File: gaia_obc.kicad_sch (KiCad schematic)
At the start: 36 parts, among them J1 USB_C_Receptacle_USB2.0_16P, J2 Micro_SD_Card_Det2, J3 Conn_01x02_Pin, J6 Conn_01x10_Pin, J7 Conn_01x10_Pin, Q1 FS8205A, U1 CD-PA1616D, U2 LGS4056H, U3 DW01A, U4 USBLC6-2P6, U5 AP2112K-3.3, U6 ESP32-S3-PICO-1-N8R2, U7 WLR089U0-I_RM

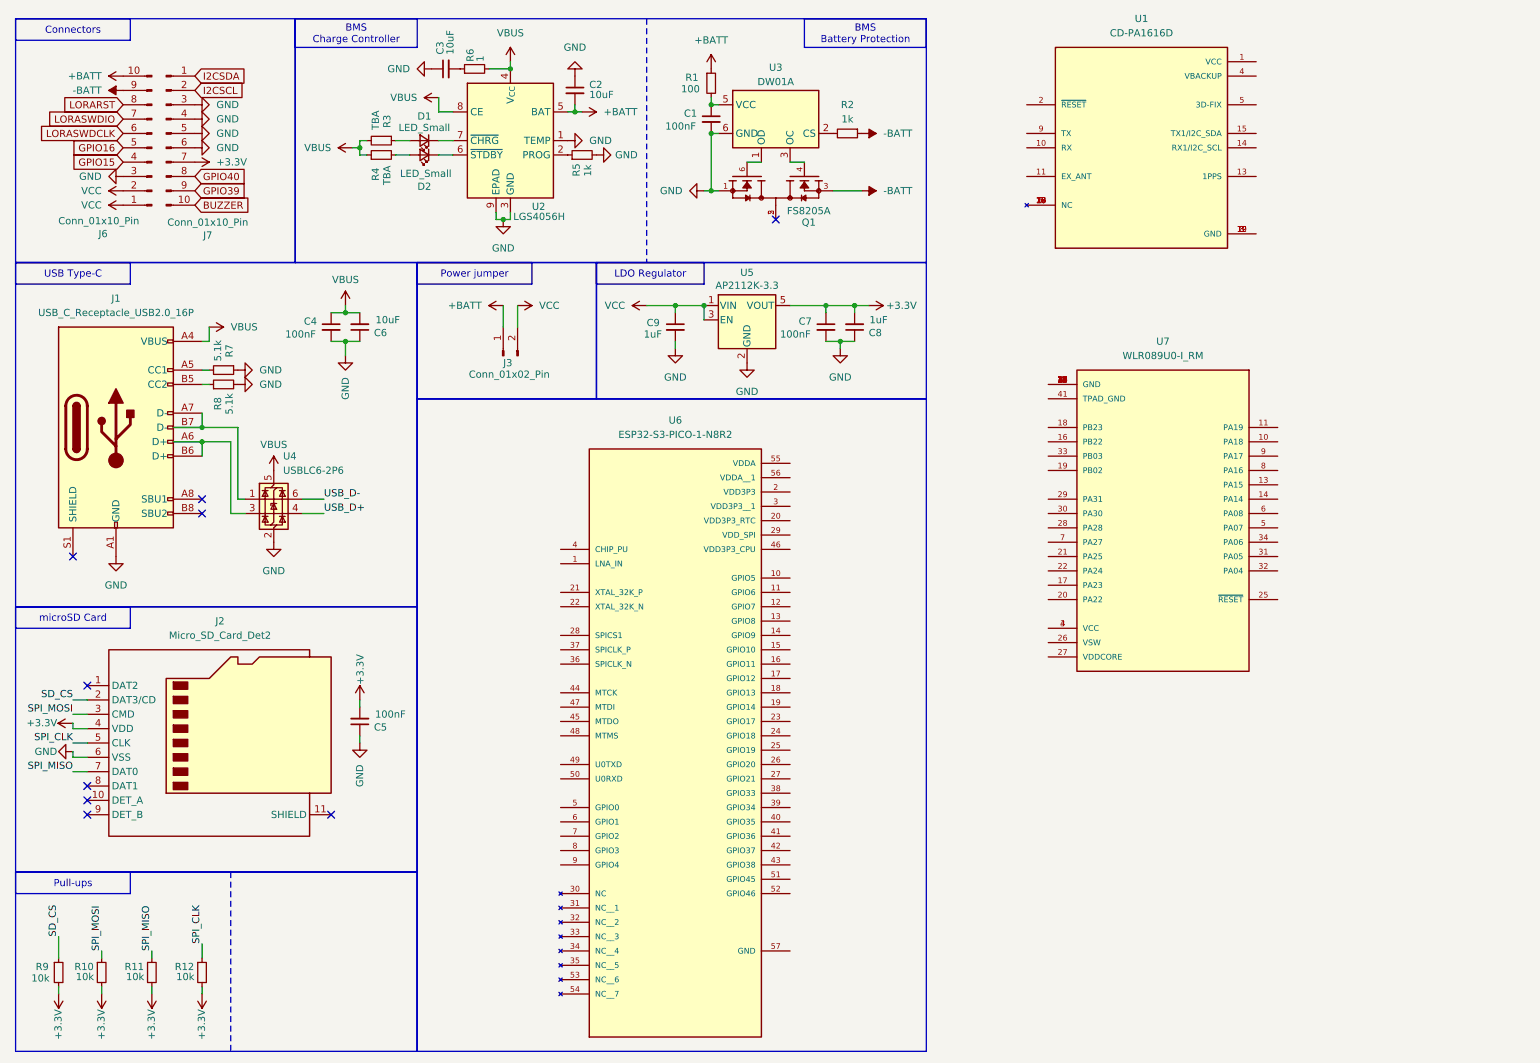
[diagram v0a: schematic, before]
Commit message: creating different sheets
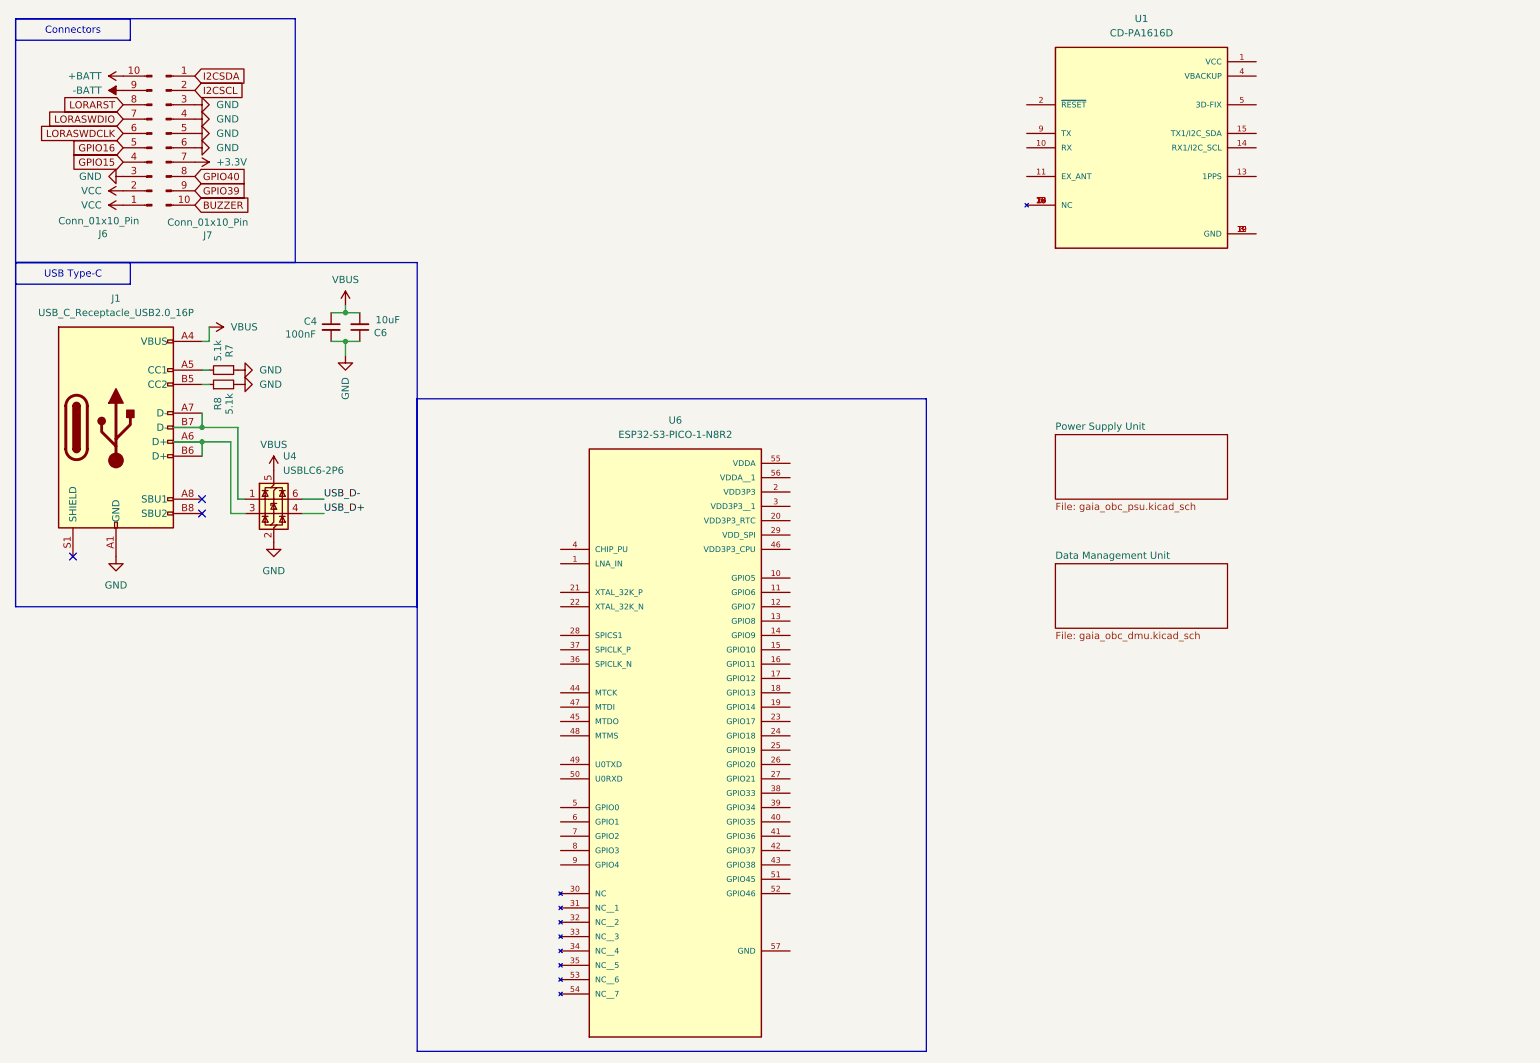
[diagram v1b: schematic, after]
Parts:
- removed C1, C5, C7: 100nF, symbol Device:C_Small
- removed C2, C3: 10uF, symbol Device:C_Small
- removed C8, C9: 1uF, symbol Device:C_Small
- removed D1, D2: LED_Small, symbol Device:LED_Small
- removed J2: Micro_SD_Card_Det2, Connector_Card:microSD_HC_Hirose_DM3D-SF, symbol Connector:Micro_SD_Card_Det2
- removed J3: Conn_01x02_Pin, Connector_Molex:Molex_MicroClasp_55935-0230_1x02_P2.00mm_Horizontal, symbol Connector:Conn_01x02_Pin
- removed Q1: FS8205A, Package_TO_SOT_SMD:SOT-23-6, symbol OnionSAT_Gaia:FS8205A
- removed R1: 100, symbol Device:R_Small
- removed R10, R11, R12, R9: 10k, symbol Device:R_Small
- removed R2, R5: 1k, symbol Device:R_Small
- removed R3, R4: TBA, symbol Device:R_Small
- removed R6: 1, symbol Device:R_Small
- removed U2: LGS4056H, Package_DFN_QFN:DFN-8-1EP_3x3mm_P0.65mm_EP1.7x2.05mm, symbol OnionSAT_Gaia:LGS4056H
- removed U3: DW01A, Package_TO_SOT_SMD:SOT-23-6, symbol Battery_Management:DW01A
- removed U5: AP2112K-3.3, Package_TO_SOT_SMD:SOT-23-5, symbol Regulator_Linear:AP2112K-3.3
- removed U7: WLR089U0-I_RM, OnionSAT_Gaia:MODULE_WLR089U0-I_RM, symbol cs25_onionsat:WLR089U0-I_RM
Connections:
- no-connect marks 9 -> 3
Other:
- added sheet Data Management Unit (gaia_obc_dmu.kicad_sch)
- added sheet Power Supply Unit (gaia_obc_psu.kicad_sch)

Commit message: almost final release
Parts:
- removed J6, J7: Conn_01x10_Pin, Connector_PinHeader_2.54mm:PinHeader_1x10_P2.54mm_Vertical_SMD_Pin1Left, symbol Connector:Conn_01x10_Pin
- removed U1: CD-PA1616D, OnionSAT_Gaia:XCVR_CD-PA1616D, symbol OnionSAT_Gaia:CD-PA1616D
- removed U6: ESP32-S3-PICO-1-N8R2, OnionSAT_Gaia:PQFN40P700X700X106-57N, symbol ESP32-S3-PICO-1-N8R2:ESP32-S3-PICO-1-N8R2
- added BZ1: Buzzer, symbol Device:Buzzer
- added C1, C10, C11, C3, C5, C7, C8, C9: 100nF, Capacitor_SMD:C_0402_1005Metric, symbol Device:C_Small
- added C12, C6: 1uF, Capacitor_SMD:C_0402_1005Metric, symbol Device:C_Small
- added J2, J3: Conn_02x10_Odd_Even, Connector_PinHeader_2.00mm:PinHeader_2x10_P2.00mm_Vertical_SMD, symbol Connector_Generic:Conn_02x10_Odd_Even
- added R1, R10, R11, R12, R13, R2, R3, R6, R7, R8, R9: 10k, symbol Device:R_Small
- added SW1, SW2: SW_Push, symbol Switch:SW_Push
- added U2: MCP23017_ML, Package_DFN_QFN:QFN-28-1EP_6x6mm_P0.65mm_EP4.25x4.25mm, symbol Interface_Expansion:MCP23017_ML
- added U3: ESP32-S3-PICO-1-N8R2, gaia_obc-footprints:PQFN40P700X700X106-57N, symbol gaia_obc-symbols:ESP32-S3-PICO-1-N8R2
- C2: renamed from C4; footprint (none) -> Capacitor_SMD:C_0402_1005Metric
- C4: renamed from C6; footprint (none) -> Capacitor_SMD:C_0402_1005Metric
- renumbered R7 to R4, R8 to R5, U4 to U1
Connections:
- net +3.3V: now also C1.2, C10.1, C11.1, C12.1, C3.1, C7.1, C8.1, C9.1, R1.1, R10.2, R11.2, R12.2, R13.2, R2.1, R3.1, R6.1, R7.2, R8.2, R9.2, U2.5 (VDD), U3.2 (VDD3P3), U3.20 (VDD3P3_RTC), U3.3 (VDD3P3), U3.46 (VDD3P3_CPU), U3.55 (VDDA), U3.56 (VDDA)
- net GND: now also BZ1.2 (-), C1.1, C10.2, C11.2, C12.2, C3.2, C5.1, C6.2, C7.2, C8.2, C9.2, SW1.1, SW2.1, U2.11 (A0), U2.12 (A1), U2.13 (A2), U2.29 (EP), U2.6 (VSS), U3.57 (GND)
- net USB_D+: now also U3.26 (GPIO20)
- net USB_D-: now also U3.25 (GPIO19)
- new net: BZ1.1 (+), U3.24 (GPIO18)
- new net: R3.2, U2.14 (~{RESET})
- new net: R1.2, U2.15 (INTB)
- new net: R2.2, U2.16 (INTA)
- new net: C5.2, C6.1, R6.2, SW1.2, U3.4 (CHIP_PU)
- new net: SW2.2, U3.5 (GPIO0)
- new net: U3.30 (NC), U3.31 (NC), U3.32 (NC), U3.33 (NC), U3.34 (NC), U3.35 (NC), U3.53 (NC), U3.54 (NC)
- new net EN_A1: U2.17 (GPA0)
- new net EN_A2: U2.18 (GPA1)
- new net EN_A3: U2.19 (GPA2)
- new net EN_B1: U2.20 (GPA3)
- new net EN_B2: U2.21 (GPA4)
- new net GPS_RX: U3.6 (GPIO1)
- new net GPS_TX: U3.7 (GPIO2)
- new net I2C_1_SCL: J2.4 (Pin_4), R8.1, U2.8 (SCK), U3.14 (GPIO9)
- new net I2C_1_SDA: J2.2 (Pin_2), R7.1, U2.9 (SDA), U3.13 (GPIO8)
- new net I2C_2_SCL: J2.3 (Pin_3), R12.1, U3.16 (GPIO11)
- new net I2C_2_SDA: J2.1 (Pin_1), R10.1, U3.15 (GPIO10)
- new net LORA_CS: U3.27 (GPIO21)
- new net LORA_RESET: U3.38 (GPIO33)
- new net PB1: U2.25 (GPB0)
- new net PB2: U2.26 (GPB1)
- new net PB3: U2.27 (GPB2)
- new net PB4: U2.28 (GPB3)
- new net PB5: U2.1 (GPB4)
- new net SCREEN_CLK: U3.9 (GPIO4)
- new net SCREEN_CS: U3.10 (GPIO5)
- new net SCREEN_DC: U3.12 (GPIO7)
- new net SCREEN_MOSI: U3.11 (GPIO6)
- new net SCREEN_RESET: U3.8 (GPIO3)
- new net SD_CS: U3.23 (GPIO17)
- new net SPI_0_MISO: R9.1, U3.17 (GPIO12)
- new net SPI_0_MOSI: R11.1, U3.18 (GPIO13)
- new net SPI_0_SCLK: R13.1, U3.19 (GPIO14)
- no-connect marks 3 -> 14
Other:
- sheet Data Management Unit ports: added GPS_RX, GPS_TX, LORA_CS, LORA_RESET, PB1, PB2, PB3, PB4, PB5, SCREEN_CLK, SCREEN_CS, SCREEN_DC, SCREEN_MOSI, SCREEN_RESET, SD_CS; removed none
- sheet Power Supply Unit ports: added EN_A1, EN_A2, EN_A3, EN_B1, EN_B2, OBC_3V0, OBC_3V3, VOUT_A1, VOUT_A2, VOUT_A3, VOUT_B1, VOUT_B2; removed none

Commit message: prep for routing 2/1
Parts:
- BZ1: footprint (none) -> gaia_obc-footprints:buzzer_MLT-5020
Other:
- moved on the sheet: BZ1, SW2
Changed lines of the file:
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@@
 	(wire
 		(pts
+			(xy 144.78 91.44) (xy 147.32 91.44)
+		)
+		(stroke
+			(width 0)
+			(type default)
+		)
+	)
+	(wire
+		(pts
 			(xy 187.96 53.34) (xy 201.93 53.34)
 		)
@@
 	(wire
 		(pts
+			(xy 144.78 90.17) (xy 144.78 91.44)
+		)
+		(stroke
+			(width 0)
+			(type default)
+		)
+	)
+	(wire
+		(pts
 			(xy 69.85 130.81) (xy 63.5 130.81)
 		)
@@
 	(wire
 		(pts
+			(xy 130.81 91.44) (xy 128.27 91.44)
+		)
+		(stroke
+			(width 0)
+			(type default)
+		)
+	)
+	(wire
+		(pts
 			(xy 41.91 88.9) (xy 46.99 88.9)
 		)
@@
 	(wire
 		(pts
-			(xy 130.81 91.44) (xy 128.27 91.44)
+			(xy 132.08 90.17) (xy 130.81 90.17)
 		)
 		(stroke
@@
 	(wire
 		(pts
-			(xy 203.2 81.28) (xy 203.2 73.66)
+			(xy 203.2 82.55) (xy 203.2 73.66)
 		)
 		(stroke
@@
 	(wire
 		(pts
-			(xy 140.97 91.44) (xy 147.32 91.44)
+			(xy 142.24 90.17) (xy 144.78 90.17)
 		)
 		(stroke
@@
 	(wire
 		(pts
+			(xy 130.81 90.17) (xy 130.81 91.44)
+		)
+		(stroke
+			(width 0)
+			(type default)
+		)
+	)
+	(wire
+		(pts
 			(xy 48.26 78.74) (xy 46.99 78.74)
 		)
@@
 	(wire
 		(pts
-			(xy 217.17 81.28) (xy 203.2 81.28)
+			(xy 234.95 82.55) (xy 203.2 82.55)
 		)
 		(stroke
@@
 	(symbol
 		(lib_id "Device:Buzzer")
-		(at 219.71 83.82 0)
+		(at 237.49 85.09 0)
 		(unit 1)
 		(exclude_from_sim no)
@@
 		(dnp no)
 		(property "Reference" "BZ1"
-			(at 220.4651 91.44 0)
+			(at 238.2451 92.71 0)
 			(effects
 				(font
@@
 		)
 		(property "Value" "Buzzer"
-			(at 220.4651 88.9 0)
+			(at 238.2451 90.17 0)
 			(effects
 				(font
@@
 			)
 		)
-		(property "Footprint" ""
-			(at 219.075 81.28 90)
+		(property "Footprint" "gaia_obc-footprints:buzzer_MLT-5020"
+			(at 236.855 82.55 90)
 			(effects
 				(font
@@
 		)
 		(property "Datasheet" "~"
-			(at 219.075 81.28 90)
+			(at 236.855 82.55 90)
 			(effects
 				(font
@@
 		)
 		(property "Description" "Buzzer, polarized"
-			(at 219.71 83.82 0)
+			(at 237.49 85.09 0)
 			(effects
 				(font
@@
 	(symbol
 		(lib_id "power:GND")
-		(at 217.17 86.36 270)
+		(at 234.95 87.63 270)
 		(unit 1)
 		(exclude_from_sim no)
@@
 		(fields_autoplaced yes)
 		(property "Reference" "#PWR032"
-			(at 210.82 86.36 0)
+			(at 228.6 87.63 0)
 			(effects
 				(font
@@
 		)
 		(property "Value" "GND"
-			(at 213.36 86.3599 90)
+			(at 231.14 87.6299 90)
 			(effects
 				(font
@@
 		)
 		(property "Footprint" ""
-			(at 217.17 86.36 0)
+			(at 234.95 87.63 0)
 			(effects
 				(font
@@
 		)
 		(property "Datasheet" ""
-			(at 217.17 86.36 0)
+			(at 234.95 87.63 0)
 			(effects
 				(font
@@
 		)
 		(property "Description" "Power symbol creates a global label with name \"GND\" , ground"
-			(at 217.17 86.36 0)
+			(at 234.95 87.63 0)
 			(effects
 				(font
@@
 	(symbol
 		(lib_id "Switch:SW_Push")
-		(at 135.89 91.44 0)
+		(at 137.16 90.17 0)
 		(unit 1)
 		(exclude_from_sim no)
@@
 		(fields_autoplaced yes)
 		(property "Reference" "SW2"
-			(at 135.89 83.82 0)
+			(at 137.16 82.55 0)
 			(effects
 				(font
@@
 		)
 		(property "Value" "SW_Push"
-			(at 135.89 86.36 0)
+			(at 137.16 85.09 0)
 			(effects
 				(font
@@
 		)
 		(property "Footprint" ""
-			(at 135.89 86.36 0)
+			(at 137.16 85.09 0)
 			(effects
 				(font
@@
 		)
 		(property "Datasheet" "~"
-			(at 135.89 86.36 0)
+			(at 137.16 85.09 0)
 			(effects
 				(font
@@
 		)
 		(property "Description" "Push button switch, generic, two pins"
-			(at 135.89 91.44 0)
+			(at 137.16 90.17 0)
 			(effects
 				(font

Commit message: almost routeable//98% done schema
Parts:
- removed C2: 100nF, Capacitor_SMD:C_0402_1005Metric, symbol Device:C_Small
- added C3: 100nF, Capacitor_SMD:C_0402_1005Metric, symbol Device:C_Small
- added D1, D2, D3, D4, D5, D6, D7, D8, D9: LED_Small, LED_SMD:LED_0603_1608Metric, symbol Device:LED_Small
- added R10, R11, R12, R20, R21, R6, R7, R8, R9: TBA, Resistor_SMD:R_0402_1005Metric, symbol Device:R_Small
- R1, R2, R3, R4, R5: footprint (none) -> Resistor_SMD:R_0402_1005Metric
- R13: renamed from R6; footprint (none) -> Resistor_SMD:R_0402_1005Metric
- R14: renamed from R7; footprint (none) -> Resistor_SMD:R_0402_1005Metric
- R15: renamed from R8; footprint (none) -> Resistor_SMD:R_0402_1005Metric
- R16: renamed from R9; footprint (none) -> Resistor_SMD:R_0402_1005Metric
- R17: renamed from R10; footprint (none) -> Resistor_SMD:R_0402_1005Metric
- R18: renamed from R11; footprint (none) -> Resistor_SMD:R_0402_1005Metric
- R19: renamed from R12; footprint (none) -> Resistor_SMD:R_0402_1005Metric
- R22: renamed from R13; footprint (none) -> Resistor_SMD:R_0402_1005Metric
- renumbered C3 to C2, U2 to U1, U1 to U2
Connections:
- net GND: now also J2.17 (Pin_17), J2.18 (Pin_18), J2.19 (Pin_19), J2.20 (Pin_20), J2.7 (Pin_7), J2.9 (Pin_9), J3.13 (Pin_13), J3.14 (Pin_14), J3.15 (Pin_15), J3.16 (Pin_16), C3.2, R10.2, R11.2, R12.2, R20.2, R21.2, R6.2, R7.2, R8.2, R9.2
- net SPI_0_MISO: now also J2.6 (Pin_6)
- net SPI_0_MOSI: now also J2.8 (Pin_8)
- net SPI_0_SCLK: now also J2.10 (Pin_10)
- net VBUS: now also C3.1, D1.2 (A)
- net at U1.2 (GPB5): now also D2.2 (A)
- net at U1.22 (GPA5): now also D5.2 (A)
- net at U1.23 (GPA6): now also D6.2 (A)
- net at U1.24 (GPA7): now also D7.2 (A)
- net at U1.3 (GPB6): now also D3.2 (A)
- net at U1.4 (GPB7): now also D4.2 (A)
- net EXP0_USART_TXD: now reaches U3.39 (GPIO34)
- net EXP0_USART_TXD: now also J2.12 (Pin_12)
- net EXP0_USART_RXD: now reaches U3.40 (GPIO35)
- net EXP0_USART_RXD: now also J2.14 (Pin_14)
- net EXP1_SPI_CS: now reaches U3.41 (GPIO36)
- net EXP1_SPI_CS: now also J2.5 (Pin_5)
- net EXP2_USART_TXD: now reaches U3.42 (GPIO37)
- net EXP2_USART_TXD: now also J2.11 (Pin_11)
- net EXP2_USART_RXD: now reaches U3.43 (GPIO38)
- net EXP2_USART_RXD: now also J2.13 (Pin_13)
- net at U3.51 (GPIO45): now also D8.2 (A)
- net at U3.52 (GPIO46): now also D9.2 (A)
- net VOUT_A1: now reaches J3.1 (Pin_1)
- net VOUT_A1: now also J3.2 (Pin_2)
- net VOUT_B2: now reaches J3.10 (Pin_10)
- net VOUT_B2: now also J3.9 (Pin_9)
- net +BATT: now reaches J3.17 (Pin_17)
- net +BATT: now also J3.18 (Pin_18)
- net -BATT: now reaches J3.19 (Pin_19)
- net -BATT: now also J3.20 (Pin_20)
- net VOUT_A2: now reaches J3.3 (Pin_3)
- net VOUT_A2: now also J3.4 (Pin_4)
- net VOUT_A3: now reaches J3.5 (Pin_5)
- net VOUT_A3: now also J3.6 (Pin_6)
- net VOUT_B1: now reaches J3.7 (Pin_7)
- net VOUT_B1: now also J3.8 (Pin_8)
- new net: D7.1 (K), R12.1
- new net: D6.1 (K), R11.1
- new net: D5.1 (K), R10.1
- new net: D2.1 (K), R7.1
- new net: D1.1 (K), R6.1
- new net: D8.1 (K), R20.1
- new net: D4.1 (K), R9.1
- new net: D9.1 (K), R21.1
- new net: D3.1 (K), R8.1
- no-connect marks 14 -> 19
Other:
- moved on the sheet: C1, C2, C5, J2, J3, R1, R14, R15, R17, R19, R2, R3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

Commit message: change screen
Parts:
- removed BZ1: Buzzer, gaia_obc-footprints:buzzer_MLT-5020, symbol Device:Buzzer
- added BZ2: Buzzer, gaia_obc-footprints:buzzer_MLT-5020, symbol Device:Buzzer
- added C45: 1uF, Capacitor_SMD:C_0402_1005Metric, symbol Device:C_Small
- added Q3: IRLML6244, Package_TO_SOT_SMD:SOT-23, symbol Transistor_FET:IRLML6244
- added R65: 1k, Resistor_SMD:R_0402_1005Metric, symbol Device:R_Small
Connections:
- net +3.3V: now also BZ2.1 (+), C45.1
- net GND: now also J1.S1 (SHIELD), C45.2, Q3.2 (S)
- net at U3.24 (GPIO18): now also R65.1
- new net: Q3.1 (G), R65.2
- new net: BZ2.2 (-), Q3.3 (D)
- no-connect marks 19 -> 18
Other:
- moved on the sheet: C10, C11, C12, C7, C8, C9

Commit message: Finalizing schematic+Start placing components
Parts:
- added AE1: Antenna, gaia_obc-footprints:ANT-SMD_L8.0-W1.0, symbol Device:Antenna
- added C46: 2,4pF, Capacitor_SMD:C_0402_1005Metric, symbol Device:C_Small
- added C47: 2,0pF, Capacitor_SMD:C_0402_1005Metric, symbol Device:C_Small
- added L1: 2,4nH, Inductor_SMD:L_0402_1005Metric, symbol Device:L_Small
- J1: footprint Connector_USB:USB_C_Receptacle_G-Switch_GT-USB-7010ASV -> gaia_obc-footprints:USB-SMD_TYPE-C-16PQT-073
- SW1, SW2: footprint (none) -> gaia_obc-footprints:KEY-SMD_L4.0-W3.0-LS4.9-1
- renumbered BZ2 to BZ1, C9 to C10, C10 to C11, C11 to C12, C12 to C13, C45 to C7, C7 to C8, C8 to C9, Q3 to Q1, R65 to R19, R19 to R20, R20 to R21, R21 to R22, R22 to R23
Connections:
- net GND: now also J1.A1B12 (GND), J1.B1A12 (GND), C46.2, C47.1; no longer J1.A1 (GND), J1.A12 (GND), J1.B1 (GND), J1.B12 (GND)
- net VBUS: now also J1.A4B9 (VBUS), J1.B4A9 (VBUS); no longer J1.A4 (VBUS), J1.A9 (VBUS), J1.B4 (VBUS), J1.B9 (VBUS)
- net at U3.1 (LNA_IN): now also C47.2, L1.2
- new net: AE1.1 (A), C46.1, L1.1
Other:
- note added: "50Ω Impedance Control"
- moved on the sheet: C5, J1, SW1

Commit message: ROUTING DONE 08. 24.
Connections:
- net EXP0_USART_RXD: now also U3.41 (GPIO36); no longer U3.40 (GPIO35)
- net EXP0_USART_TXD: now also U3.42 (GPIO37); no longer U3.39 (GPIO34)
- net EXP1_SPI_CS: now also U3.43 (GPIO38); no longer U3.41 (GPIO36)
- net EXP2_USART_RXD: now also U3.39 (GPIO34); no longer U3.43 (GPIO38)
- net EXP2_USART_TXD: now also U3.40 (GPIO35); no longer U3.42 (GPIO37)
- net SCREEN_CLK: now also U3.11 (GPIO6); no longer U3.9 (GPIO4)
- net SCREEN_CS: now also U3.8 (GPIO3); no longer U3.10 (GPIO5)
- net SCREEN_DC: now also U3.10 (GPIO5); no longer U3.12 (GPIO7)
- net SCREEN_MOSI: now also U3.12 (GPIO7); no longer U3.11 (GPIO6)
- net SCREEN_RESET: now also U3.9 (GPIO4); no longer U3.8 (GPIO3)
- net at U1.22 (GPA5): now also D7.2 (A); no longer D5.2 (A)
- net at U1.24 (GPA7): now also D5.2 (A); no longer D7.2 (A)
- net at U1.3 (GPB6): now also D4.2 (A); no longer D3.2 (A)
- net at U1.4 (GPB7): now also D3.2 (A); no longer D4.2 (A)
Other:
- moved on the sheet: D3, D4, D5, D6, D7, R10, R12, R8, R9

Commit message: finalizing everything + creating stencil + ORDER 08. 25.
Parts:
- J2, J3: footprint Connector_PinHeader_2.00mm:PinHeader_2x10_P2.00mm_Vertical_SMD -> gaia_obc-footprints:PinHeader_2x10_P2.00mm_Vertical_SMD
- Q1: footprint Package_TO_SOT_SMD:SOT-23 -> gaia_obc-footprints:SOT-23
- U1: footprint Package_DFN_QFN:QFN-28-1EP_6x6mm_P0.65mm_EP4.25x4.25mm -> gaia_obc-footprints:QFN-28-1EP_6x6mm_P0.65mm_EP4.25x4.25mm
- U2: footprint Package_TO_SOT_SMD:SOT-666 -> gaia_obc-footprints:SOT-666
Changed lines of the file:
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@@
 			)
 		)
-		(property "Footprint" "Package_DFN_QFN:QFN-28-1EP_6x6mm_P0.65mm_EP4.25x4.25mm"
+		(property "Footprint" "gaia_obc-footprints:QFN-28-1EP_6x6mm_P0.65mm_EP4.25x4.25mm"
 			(at 63.5 186.69 0)
 			(effects
@@
 			)
 		)
-		(property "Footprint" "Package_TO_SOT_SMD:SOT-23"
+		(property "Footprint" "gaia_obc-footprints:SOT-23"
 			(at 243.84 86.995 0)
 			(effects
@@
 			)
 		)
-		(property "Footprint" "Package_TO_SOT_SMD:SOT-666"
+		(property "Footprint" "gaia_obc-footprints:SOT-666"
 			(at 60.706 105.791 0)
 			(effects
@@
 			)
 		)
-		(property "Footprint" "Connector_PinHeader_2.00mm:PinHeader_2x10_P2.00mm_Vertical_SMD"
+		(property "Footprint" "gaia_obc-footprints:PinHeader_2x10_P2.00mm_Vertical_SMD"
 			(at 85.09 38.1 0)
 			(effects
@@
 			)
 		)
-		(property "Footprint" "Connector_PinHeader_2.00mm:PinHeader_2x10_P2.00mm_Vertical_SMD"
+		(property "Footprint" "gaia_obc-footprints:PinHeader_2x10_P2.00mm_Vertical_SMD"
 			(at 40.64 38.1 0)
 			(effects
